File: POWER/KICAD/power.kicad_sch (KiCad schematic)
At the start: 0 parts

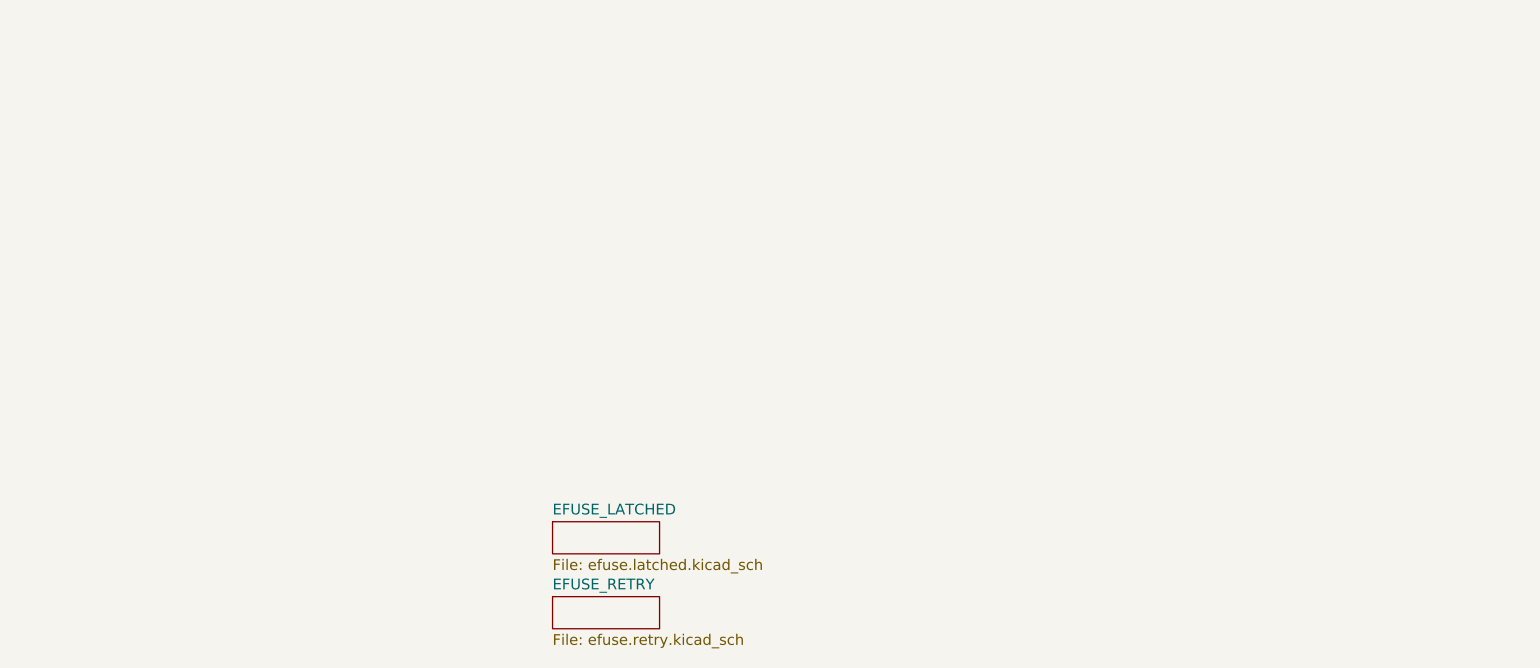
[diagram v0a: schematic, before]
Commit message: Updated Power Schematic / Kicad
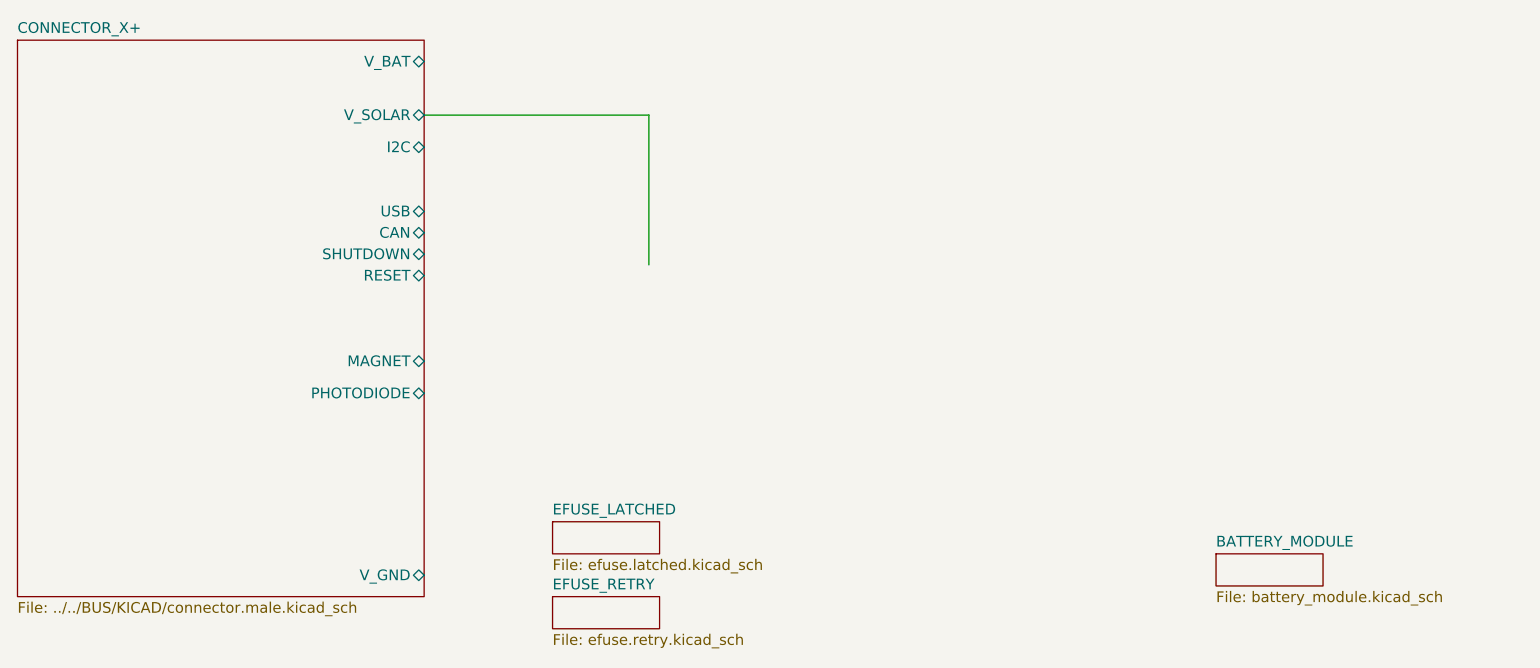
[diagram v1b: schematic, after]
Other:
- added sheet BATTERY_MODULE (battery_module.kicad_sch)
- added sheet CONNECTOR_X+ (../../BUS/KICAD/connector.male.kicad_sch)
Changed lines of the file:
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@@
 	(generator_version "8.0")
 	(paper "A4")
+	(wire
+		(pts
+			(xy 134.62 44.45) (xy 107.95 44.45)
+		)
+		(stroke
+			(width 0)
+			(type default)
+		)
+	)
+	(wire
+		(pts
+			(xy 134.62 62.23) (xy 134.62 44.45)
+		)
+		(stroke
+			(width 0)
+			(type default)
+		)
+	)
+	(sheet
+		(at 59.69 35.56)
+		(size 48.26 66.04)
+		(fields_autoplaced yes)
+		(stroke
+			(width 0.1524)
+			(type solid)
+		)
+		(fill
+			(color 0 0 0 0.0000)
+		)
+		(property "Sheetname" "CONNECTOR_X+"
+			(at 59.69 34.8484 0)
+			(effects
+				(font
+					(size 1.27 1.27)
+				)
+				(justify left bottom)
+			)
+		)
+		(property "Sheetfile" "../../BUS/KICAD/connector.male.kicad_sch"
+			(at 59.69 102.1846 0)
+			(effects
+				(font
+					(size 1.27 1.27)
+				)
+				(justify left top)
+			)
+		)
+		(pin "RESET" bidirectional
+			(at 107.95 63.5 0)
+			(effects
+				(font
+					(size 1.27 1.27)
+				)
+				(justify right)
+			)
+		)
+		(pin "V_GND" bidirectional
+			(at 107.95 99.06 0)
+			(effects
+				(font
+					(size 1.27 1.27)
+				)
+				(justify right)
+			)
+		)
+		(pin "V_SOLAR" bidirectional
+			(at 107.95 44.45 0)
+			(effects
+				(font
+					(size 1.27 1.27)
+				)
+				(justify right)
+			)
+		)
+		(pin "V_BAT" bidirectional
+			(at 107.95 38.1 0)
+			(effects
+				(font
+					(size 1.27 1.27)
+				)
+				(justify right)
+			)
+		)
+		(pin "SHUTDOWN" bidirectional
+			(at 107.95 60.96 0)
+			(effects
+				(font
+					(size 1.27 1.27)
+				)
+				(justify right)
+			)
+		)
+		(pin "USB" bidirectional
+			(at 107.95 55.88 0)
+			(effects
+				(font
+					(size 1.27 1.27)
+				)
+				(justify right)
+			)
+		)
+		(pin "MAGNET" bidirectional
+			(at 107.95 73.66 0)
+			(effects
+				(font
+					(size 1.27 1.27)
+				)
+				(justify right)
+			)
+		)
+		(pin "PHOTODIODE" bidirectional
+			(at 107.95 77.47 0)
+			(effects
+				(font
+					(size 1.27 1.27)
+				)
+				(justify right)
+			)
+		)
+		(pin "I2C" bidirectional
+			(at 107.95 48.26 0)
+			(effects
+				(font
+					(size 1.27 1.27)
+				)
+				(justify right)
+			)
+		)
+		(pin "CAN" bidirectional
+			(at 107.95 58.42 0)
+			(effects
+				(font
+					(size 1.27 1.27)
+				)
+				(justify right)
+			)
+		)
+		(instances
+			(project "power"
+				(path "/ef47adc1-536f-4520-9ebd-fa1d01e89711"
+					(page "5")
+				)
+			)
+		)
+	)
 	(sheet
 		(at 123.19 101.6)
@@
 				)
 			)
+		)
+	)
+	(sheet
+		(at 201.93 96.52)
+		(size 12.7 3.81)
+		(fields_autoplaced yes)
+		(stroke
+			(width 0.1524)
+			(type solid)
+		)
+		(fill
+			(color 0 0 0 0.0000)
+		)
+		(property "Sheetname" "BATTERY_MODULE"
+			(at 201.93 95.8084 0)
+			(effects
+				(font
+					(size 1.27 1.27)
+				)
+				(justify left bottom)
+			)
+		)
+		(property "Sheetfile" "battery_module.kicad_sch"
+			(at 201.93 100.9146 0)
+			(effects
+				(font
+					(size 1.27 1.27)
+				)
+				(justify left top)
+			)
+		)
+		(instances
+			(project "power"
+				(path "/ef47adc1-536f-4520-9ebd-fa1d01e89711"
+					(page "3")
+				)
+			)

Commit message: schematic design
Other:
- sheet BATTERY_MODULE renamed POWER_MODULE
- sheet POWER_MODULE: file battery_module.kicad_sch -> power.module.kicad_sch
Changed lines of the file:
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@@
 			(color 0 0 0 0.0000)
 		)
-		(property "Sheetname" "BATTERY_MODULE"
+		(property "Sheetname" "POWER_MODULE"
 			(at 201.93 95.8084 0)
 			(effects
@@
 			)
 		)
-		(property "Sheetfile" "battery_module.kicad_sch"
+		(property "Sheetfile" "power.module.kicad_sch"
 			(at 201.93 100.9146 0)
 			(effects
